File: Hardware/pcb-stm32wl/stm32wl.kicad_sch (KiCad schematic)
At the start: 22 parts, among them U5 STM32WL55CCU6, X1 32MHz, Y1 32.768KHz

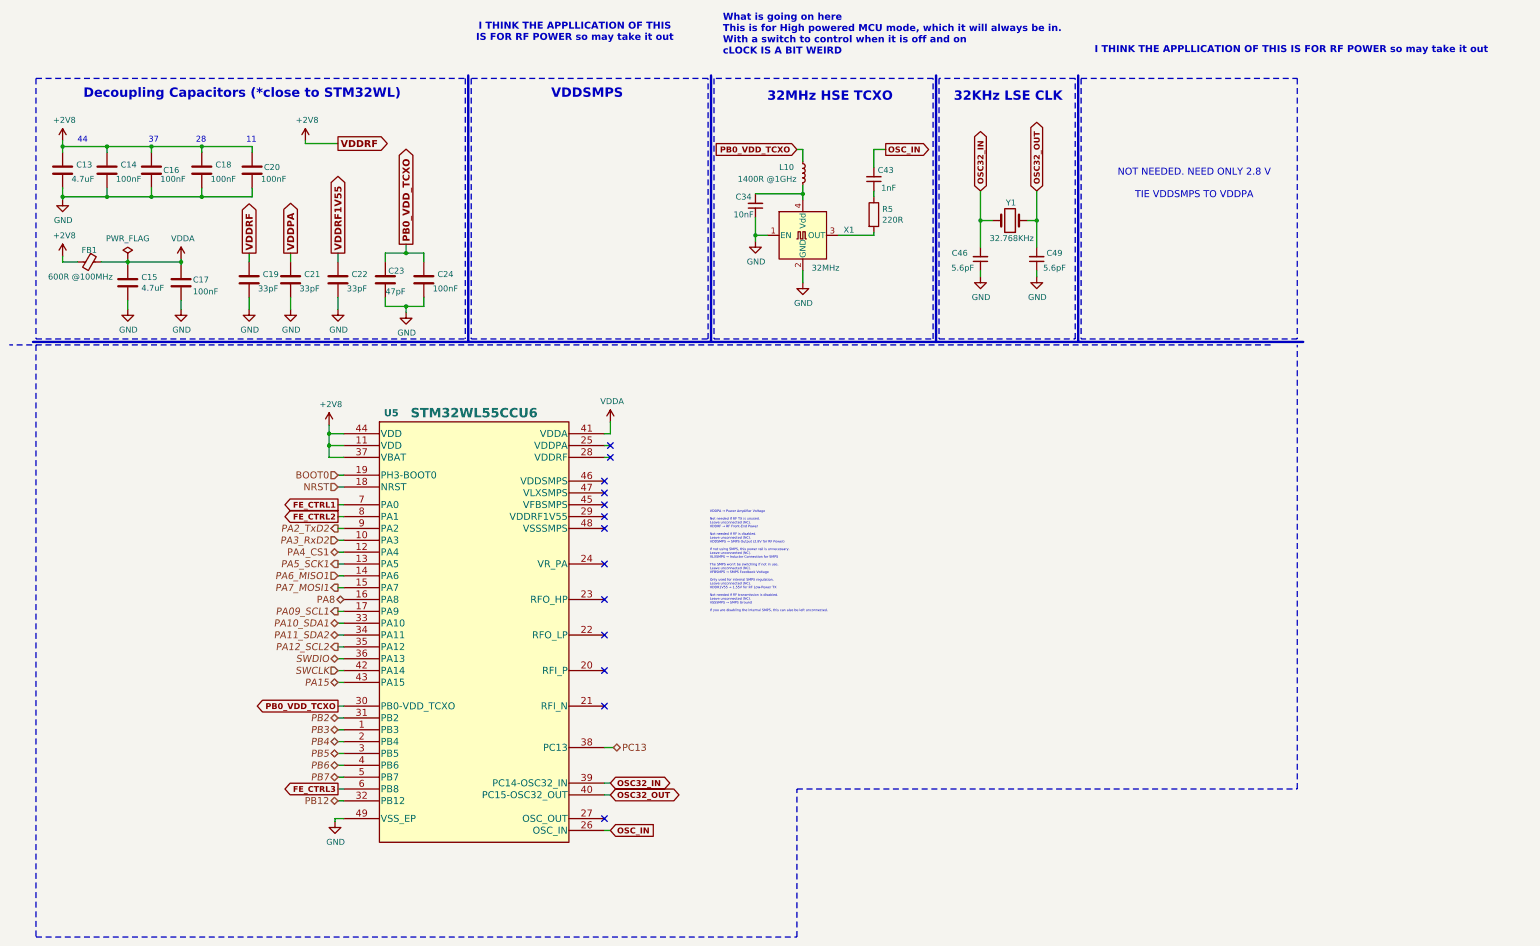
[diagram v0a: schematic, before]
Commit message: added newly selected components into kicadImports folder
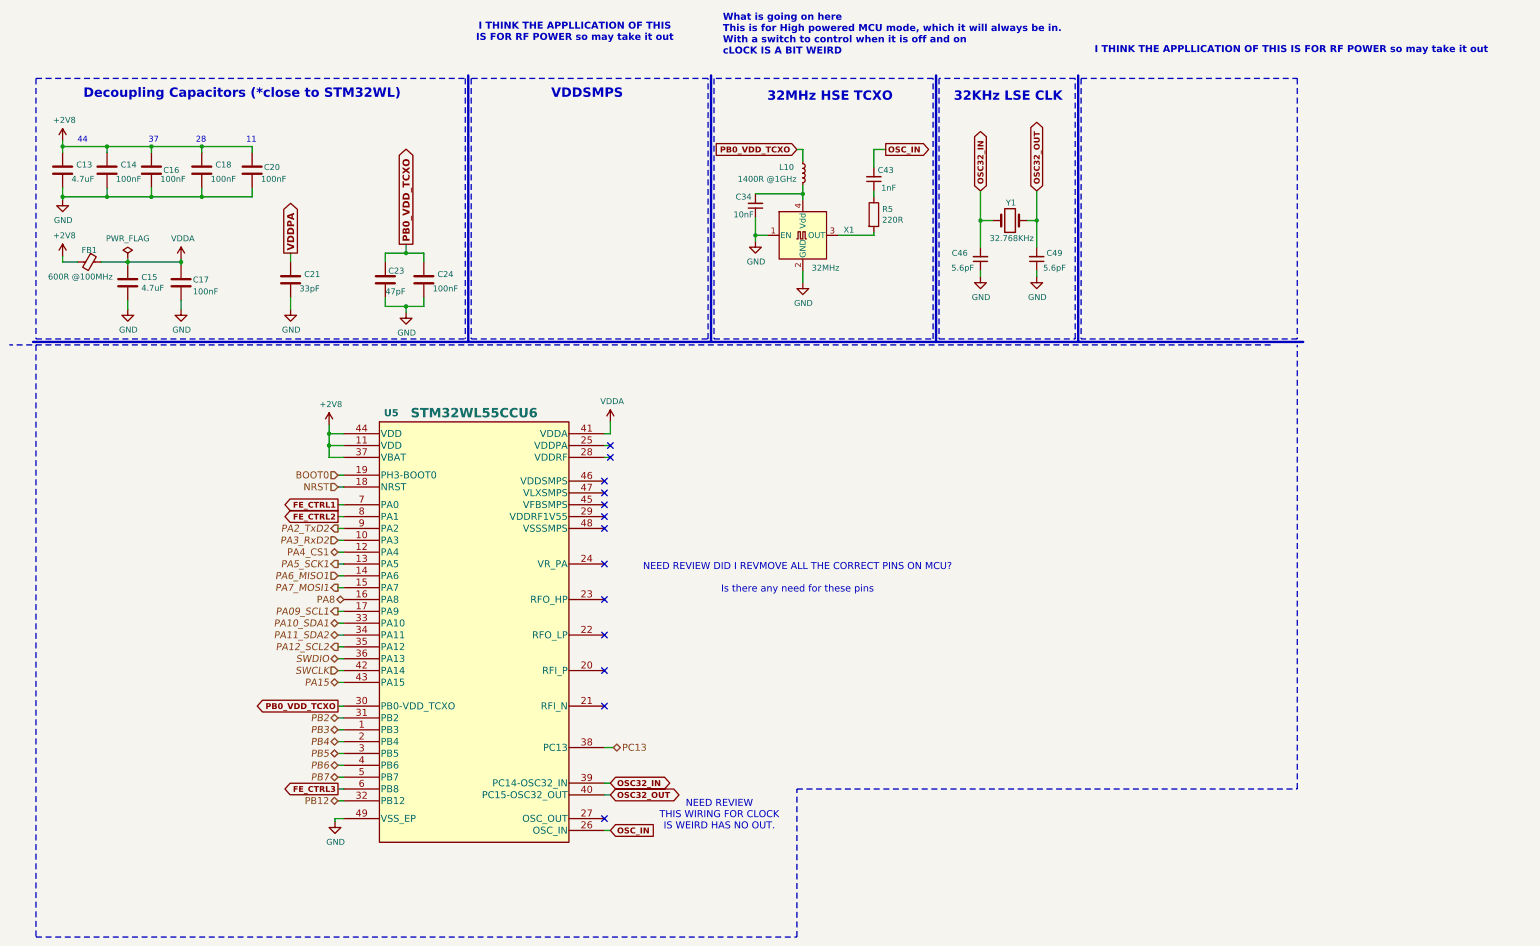
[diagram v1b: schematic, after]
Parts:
- removed C19, C22: 33pF, Capacitor_SMD:C_0402_1005Metric, symbol Device:C
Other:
- note added: "NEED REVIEW DID I REVMOVE ALL THE CORRECT PINS ON MCU? Is there any need for these pins"
- note added: "NEED REVIEW THIS WIRING FOR CLOCK IS WEIRD HAS NO OUT."
- note removed: "NOT NEEDED. NEED ONLY 2.8 V TIE VDDSMPS TO VDDPA"
- note removed: "VDDPA → Power Amplifier Voltage Not needed if RF TX is unused. Leave unconnected (NC). VDDRF → RF Front-End Power Not needed if RF is disabled. Leave unconnected (NC). VDDSMPS → SMPS Output (2.8V for RF Power) If not using SMPS, this power rail is unnecessary. Leave unconnected (NC). VLXSMPS → Inductor Connection for SMPS The SMPS won't be switching if not in use. Leave unconnected (NC). VFBSMPS 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"
